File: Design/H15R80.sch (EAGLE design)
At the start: 24 parts, among them P1 HEXABIT_17.32_NO_P3_P6, U1 STM32F091CBU6, U2 DAC8760IRHAR, X1 XTALL_CSTCE8M00G52

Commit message: Finished schematics
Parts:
- added C12, C15: 10.0uF, rcl:CPOL-USCT7343
- added C13, C16, C18, C19, C20, C22, C25, C31, C33: 100nF, Hexabitz:C-0603
- added C14, C17, C21, C23, C24, C32, C34: 100pF, Hexabitz:C-0603
- added C26, C27, C28, C29: DNP, Hexabitz:C-0603
- added C30: 22nF, Hexabitz:C-0603
- added R5: 10.0K, Hexabitz:R-0603
- added R6: 15.0K, Hexabitz:R-0603
- added U3: OPA192, Hexabitz:OPA192IDBVR
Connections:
- removed net UART1_RX: U1.PA10
- removed net UART1_TX: U1.PA9
- removed net UART2_RX: U1.PA3
- removed net UART2_TX: U1.PA2
- new net +15V: C12.+, C13.1, C14.1, C20.1, C21.1, C26.2, C27.2, C31.1, C32.1, PWR-3.K, U2.AVDD, U3.V+
- new net -15V: C15.-, C16.1, C17.1, C22.1, C23.1, C24.1, C25.1, C33.1, C34.1, PWR-1.K, U2.AVSS, U2.AVSS_2, U2.PAD, U3.V-
- new net AGND: AO-2.K, C12.-, C13.2, C14.2, C15.+, C16.2, C17.2, C18.2, C19.2, C20.2, C21.2, C22.2, C23.2, C24.2, C25.2, C29.1, C30.2, C31.2, C32.2, C33.2, C34.2, PWR-2.K, R6.1, U2.-VSENSE, U2.CLR, U2.CLR-SEL, U2.DVDD-EN, U2.GND, U2.GND_2, U2.GND_3, U2.GND_4
- new net AO_ALARM: R5.1, U1.PA8, U2.ALARM_N
- new net N$1: AO-1.K, C28.2, C29.2, U2.IOUT, U2.VOUT, U3.IN+
- new net N$10: C27.1, U2.CAP1
- new net N$11: C28.1, U2.CMP
- new net N$12: R6.2, U2.ISET-R
- new net N$13: U2.+VSENSE, U3.IN-, U3.OUT
- new net N$14: C30.1, U2.HART-IN
- new net N$2: C19.1, U2.REFIN, U2.REFOUT
- new net N$8: C26.1, U2.CAP2
- new net SPI2_CS: U1.PB12, U2.LATCH
- new net SPI2_MISO: U1.PB14, U2.SDO
- new net SPI2_MOSI: U1.PB15, U2.DIN
- new net SPI2_SCK: U1.PB13, U2.SCLK
- new net UART1_RX*: P1.SD5, U1.PA10
- new net UART1_TX*: P1.SU5, U1.PA9
- new net UART2_RX*: P1.SD2, U1.PA3
- new net UART2_TX*: P1.SU2, U1.PA2
- net UART3_RX: now also P1.SD4
- net UART3_TX: now also P1.SU4
- net UART5_RX: now also P1.SD1
- net UART5_TX: now also P1.SU1
- net VDD: now also C18.1, R5.2, U2.DVDD
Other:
- note added: "Hi-precision Voltage & Current Analog Output"
- note removed: "Voltage & Current Analog Output"
- moved on the sheet: AO-1, AO-2, PWR-1, PWR-2, PWR-3

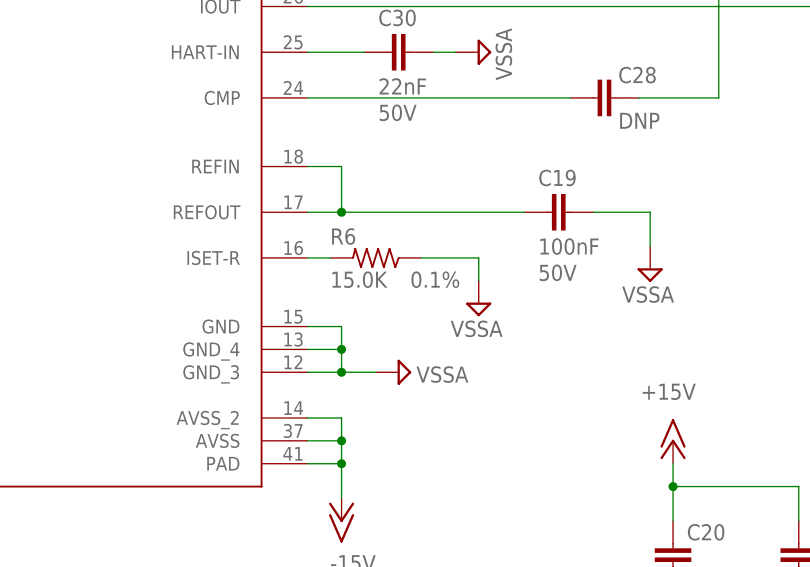
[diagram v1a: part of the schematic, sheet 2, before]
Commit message: Placed most components Routed analog routes
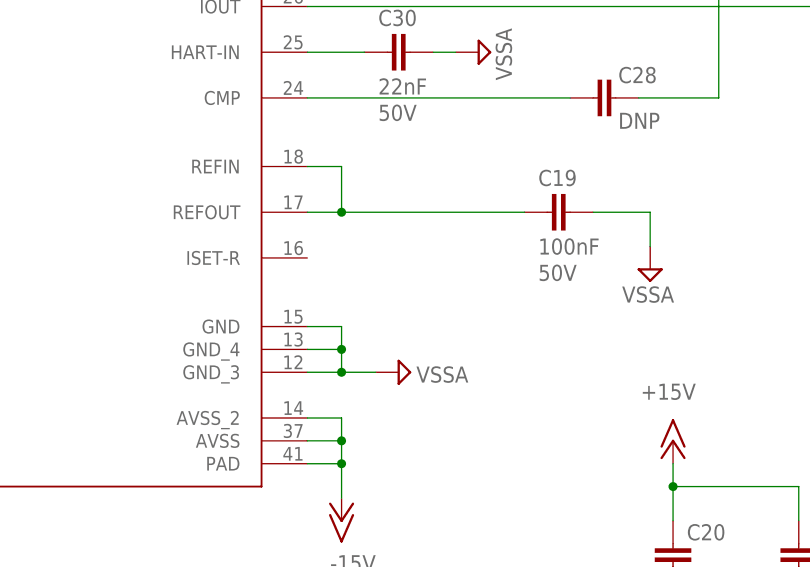
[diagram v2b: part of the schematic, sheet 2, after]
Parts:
- removed R6: 15.0K, Hexabitz:R-0603
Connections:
- removed net N$12: R6.2, U2.ISET-R
- net AGND: no longer R6.1
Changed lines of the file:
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@@
 <part name="SUPPLY28" library="supply2" deviceset="AGND" device="" value="VSSA"/>
 <part name="SUPPLY29" library="supply2" deviceset="AGND" device="" value="VSSA"/>
-<part name="R6" library="Hexabitz" deviceset="R-0603" device="" value="15.0K">
-<attribute name="MFN" value="Susumu"/>
-<attribute name="MPN" value="RG1608P-153-B-T5"/>
-<attribute name="OCTOPART_URL" value="https://octopart.com/rg1608p-153-b-t5-susumu-1191833?r=sp&amp;s=-o8BbZPwS5yNTzBtGupR8A"/>
-<attribute name="RESISTANCE" value="15.0 kOhm"/>
-<attribute name="TOLERANCE" value="0.1%"/>
-</part>
-<part name="SUPPLY30" library="supply2" deviceset="AGND" device="" value="VSSA"/>
 <part name="SUPPLY31" library="supply2" deviceset="AGND" device="" value="VSSA"/>
 <part name="C30" library="Hexabitz" deviceset="C-0603" device="" value="22nF">
@@
 <text x="116.84" y="95.25" size="1.778" layer="95">VDDA Coupling</text>
 <text x="153.67" y="95.25" size="1.778" layer="95">VDDIO2 Coupling</text>
-<text x="195.58" y="95.25" size="1.778" layer="95">VDD Coupling</text>
+<text x="193.04" y="95.25" size="1.778" layer="95">VDD Coupling</text>
 <text x="229.87" y="95.25" size="1.778" layer="95">VBAT</text>
 <text x="0" y="-0.127" size="0.0508" layer="205" font="vector">C:/Users/Admin/Desktop/logodraft.bmp</text>
@@
 </instance>
 <instance part="SUPPLY8" gate="G$1" x="156.21" y="87.63" smashed="yes">
-<attribute name="VALUE" x="159.385" y="92.075" size="1.778" layer="96" rot="R180"/>
+<attribute name="VALUE" x="154.305" y="90.805" size="1.778" layer="96"/>
 </instance>
 <instance part="GND2" gate="1" x="156.21" y="69.85" smashed="yes">
@@
 </instance>
 <instance part="SUPPLY10" gate="G$1" x="190.5" y="87.63" smashed="yes">
-<attribute name="VALUE" x="193.675" y="92.075" size="1.778" layer="96" rot="R180"/>
+<attribute name="VALUE" x="188.595" y="90.805" size="1.778" layer="96"/>
 </instance>
 <instance part="SUPPLY13" gate="G$1" x="232.41" y="87.63" smashed="yes">
-<attribute name="VALUE" x="235.585" y="92.075" size="1.778" layer="96" rot="R180"/>
+<attribute name="VALUE" x="230.505" y="90.805" size="1.778" layer="96"/>
 </instance>
 <instance part="SUPPLY12" gate="G$1" x="203.2" y="109.22" smashed="yes" rot="R90">
@@
 <attribute name="VALUE" x="93.345" y="142.113" size="1.778" layer="96" rot="R90"/>
 </instance>
-<instance part="R6" gate="G$1" x="156.21" y="81.28" smashed="yes" rot="R180">
-<attribute name="NAME" x="151.13" y="82.7786" size="1.778" layer="95"/>
-<attribute name="VALUE" x="151.13" y="77.978" size="1.778" layer="96"/>
-<attribute name="TOLERANCE" x="160.02" y="77.978" size="1.778" layer="96"/>
-</instance>
-<instance part="SUPPLY30" gate="G$1" x="167.64" y="76.2" smashed="yes">
-<attribute name="VALUE" x="170.307" y="74.295" size="1.778" layer="96" rot="R180"/>
-</instance>
 <instance part="SUPPLY31" gate="G$1" x="158.75" y="144.78" smashed="yes" rot="R90">
 <attribute name="VALUE" x="160.655" y="147.447" size="1.778" layer="96" rot="R270"/>
@@
 </segment>
 <segment>
-<pinref part="R6" gate="G$1" pin="1"/>
-<pinref part="SUPPLY30" gate="G$1" pin="AGND"/>
-<wire x1="167.64" y1="78.74" x2="167.64" y2="81.28" width="0.1524" layer="91"/>
-<wire x1="167.64" y1="81.28" x2="161.29" y2="81.28" width="0.1524" layer="91"/>
-</segment>
-<segment>
 <pinref part="U2" gate="A" pin="-VSENSE"/>
 <pinref part="SUPPLY31" gate="G$1" pin="AGND"/>
@@
 </segment>
 </net>
-<net name="N$12" class="0">
-<segment>
-<pinref part="U2" gate="A" pin="ISET-R"/>
-<pinref part="R6" gate="G$1" pin="2"/>
-<wire x1="151.13" y1="81.28" x2="148.59" y2="81.28" width="0.1524" layer="91"/>
-</segment>
-</net>
 <net name="N$13" class="0">
 <segment>
@@
 </sheet>
 </sheets>
+<errors>
+</errors>
 </schematic>
 </drawing>

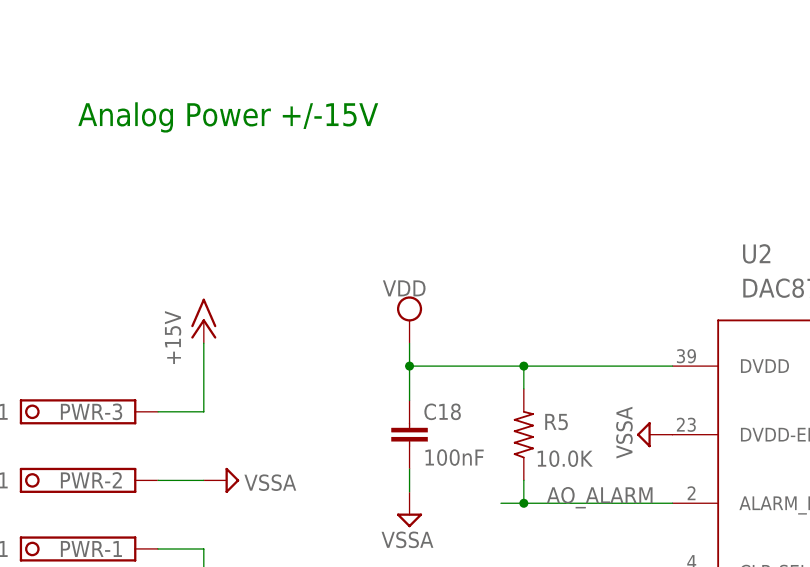
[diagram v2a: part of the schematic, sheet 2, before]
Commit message: Routing digital section
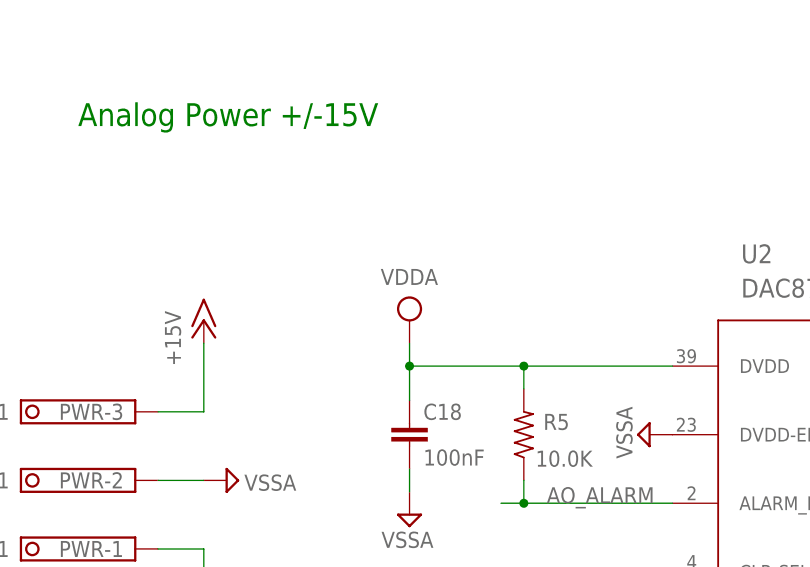
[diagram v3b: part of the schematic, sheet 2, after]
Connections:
- removed net AGND: AO-2.K, C12.-, C13.2, C14.2, C15.+, C16.2, C17.2, C18.2, C19.2, C20.2, C21.2, C22.2, C23.2, C24.2, C25.2, C29.1, C30.2, C31.2, C32.2, C33.2, C34.2, PWR-2.K, U2.-VSENSE, U2.CLR, U2.CLR-SEL, U2.DVDD-EN, U2.GND, U2.GND_2, U2.GND_3, U2.GND_4
- net VDD: no longer C18.1, R5.2, U2.DVDD
- net VDDA: now also C18.1, R5.2, U2.DVDD
- net VSSA: now also AO-2.K, C12.-, C13.2, C14.2, C15.+, C16.2, C17.2, C18.2, C19.2, C20.2, C21.2, C22.2, C23.2, C24.2, C25.2, C29.1, C30.2, C31.2, C32.2, C33.2, C34.2, PWR-2.K, U2.-VSENSE, U2.CLR, U2.CLR-SEL, U2.DVDD-EN, U2.GND, U2.GND_2, U2.GND_3, U2.GND_4
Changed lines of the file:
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@@
 <attribute name="VOLTAGE_RATING" value="10V"/>
 </part>
-<part name="SUPPLY20" library="supply2" deviceset="VDD" device=""/>
 <part name="R5" library="Hexabitz" deviceset="R-0603" device="" value="10.0K">
 <attribute name="MFN" value="Yageo"/>
@@
 <part name="SUPPLY34" library="supply2" deviceset="AGND" device="" value="VSSA"/>
 <part name="P-6" library="supply1" library_urn="urn:adsk.eagle:library:371" deviceset="-15V" device=""/>
+<part name="SUPPLY14" library="supply2" deviceset="VCC" device="" value="VDDA"/>
 </parts>
 <sheets>
@@
 <attribute name="VALUE" x="70.104" y="141.351" size="1.778" layer="96"/>
 </instance>
-<instance part="SUPPLY20" gate="G$1" x="68.58" y="157.48" smashed="yes">
-<attribute name="VALUE" x="70.485" y="161.925" size="1.778" layer="96" rot="R180"/>
-</instance>
 <instance part="R5" gate="G$1" x="81.28" y="144.78" smashed="yes" rot="R90">
 <attribute name="NAME" x="86.36" y="147.0914" size="1.778" layer="95" rot="R180"/>
@@
 <attribute name="VALUE" x="246.38" y="176.53" size="1.778" layer="96"/>
 </instance>
+<instance part="SUPPLY14" gate="G$1" x="68.58" y="157.48" smashed="yes">
+<attribute name="VALUE" x="71.755" y="163.195" size="1.778" layer="96" rot="R180"/>
+</instance>
 </instances>
 <busses>
@@
 </segment>
 </net>
-<net name="AGND" class="0">
+<net name="VSSA" class="0">
 <segment>
 <pinref part="PWR" gate="-2" pin="K"/>
@@
 </segment>
 </net>
-<net name="VDD" class="0">
-<segment>
-<pinref part="SUPPLY20" gate="G$1" pin="VDD"/>
-<pinref part="C18" gate="G$1" pin="1"/>
-<wire x1="68.58" y1="154.94" x2="68.58" y2="152.4" width="0.1524" layer="91"/>
-<pinref part="U2" gate="A" pin="DVDD"/>
-<wire x1="68.58" y1="152.4" x2="68.58" y2="148.59" width="0.1524" layer="91"/>
-<wire x1="97.79" y1="152.4" x2="81.28" y2="152.4" width="0.1524" layer="91"/>
-<junction x="68.58" y="152.4"/>
-<pinref part="R5" gate="G$1" pin="2"/>
-<wire x1="81.28" y1="152.4" x2="68.58" y2="152.4" width="0.1524" layer="91"/>
-<wire x1="81.28" y1="149.86" x2="81.28" y2="152.4" width="0.1524" layer="91"/>
-<junction x="81.28" y="152.4"/>
-</segment>
-</net>
 <net name="AO_ALARM" class="0">
 <segment>
@@
 </segment>
 </net>
+<net name="VDDA" class="0">
+<segment>
+<pinref part="C18" gate="G$1" pin="1"/>
+<wire x1="68.58" y1="154.94" x2="68.58" y2="152.4" width="0.1524" layer="91"/>
+<pinref part="U2" gate="A" pin="DVDD"/>
+<wire x1="68.58" y1="152.4" x2="68.58" y2="148.59" width="0.1524" layer="91"/>
+<wire x1="97.79" y1="152.4" x2="81.28" y2="152.4" width="0.1524" layer="91"/>
+<junction x="68.58" y="152.4"/>
+<pinref part="R5" gate="G$1" pin="2"/>
+<wire x1="81.28" y1="152.4" x2="68.58" y2="152.4" width="0.1524" layer="91"/>
+<wire x1="81.28" y1="149.86" x2="81.28" y2="152.4" width="0.1524" layer="91"/>
+<junction x="81.28" y="152.4"/>
+<pinref part="SUPPLY14" gate="G$1" pin="VCC"/>
+</segment>
+</net>

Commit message: Finished routing and silkscreen placement
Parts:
- U2: value DAC8760IRHAR -> DAC8760RHA
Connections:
- net GND: now also U1.PA15, U1.PA6, U1.PA7, U1.PB0, U1.PB1, U1.PB2, U1.PB5, U1.PB6, U1.PB7, U1.PC13, U1.PC14-OSC32_IN, U1.PC15-OSC32_OUT
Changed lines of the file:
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@@
 <attribute name="OCTOPART_URL" value="https://octopart.com/1751251-phoenix+contact-36473?r=sp&amp;s=9M0VWNoHTyq04j3qI6lQOQ "/>
 </part>
-<part name="U2" library="Hexabitz" deviceset="DAC7760IRHAR" device="" value="DAC8760IRHAR"/>
+<part name="U2" library="Hexabitz" deviceset="DAC7760IRHAR" device="" value="DAC8760RHA"/>
 <part name="SUPPLY15" library="supply2" deviceset="AGND" device="" value="VSSA"/>
 <part name="P+1" library="supply1" library_urn="urn:adsk.eagle:library:371" deviceset="+15V" device=""/>
@@
 <part name="P-6" library="supply1" library_urn="urn:adsk.eagle:library:371" deviceset="-15V" device=""/>
 <part name="SUPPLY14" library="supply2" deviceset="VCC" device="" value="VDDA"/>
+<part name="GND9" library="supply1" deviceset="GND" device=""/>
+<part name="GND10" library="supply1" deviceset="GND" device=""/>
+<part name="GND11" library="supply1" deviceset="GND" device=""/>
+<part name="GND12" library="supply1" deviceset="GND" device=""/>
 </parts>
 <sheets>
@@
 <attribute name="VALUE" x="43.815" y="98.425" size="1.778" layer="96"/>
 </instance>
+<instance part="GND9" gate="1" x="120.65" y="162.56" smashed="yes" rot="R270">
+<attribute name="VALUE" x="118.11" y="165.1" size="1.778" layer="96" rot="R270"/>
+</instance>
+<instance part="GND10" gate="1" x="198.12" y="177.8" smashed="yes" rot="R90">
+<attribute name="VALUE" x="200.66" y="175.26" size="1.778" layer="96" rot="R90"/>
+</instance>
+<instance part="GND11" gate="1" x="129.54" y="132.08" smashed="yes" rot="R270">
+<attribute name="VALUE" x="127" y="134.62" size="1.778" layer="96" rot="R270"/>
+</instance>
+<instance part="GND12" gate="1" x="198.12" y="162.56" smashed="yes" rot="R90">
+<attribute name="VALUE" x="200.66" y="160.02" size="1.778" layer="96" rot="R90"/>
+</instance>
 </instances>
 <busses>
@@
 <junction x="45.72" y="111.76"/>
 </segment>
+<segment>
+<pinref part="GND9" gate="1" pin="GND"/>
+<pinref part="U1" gate="G$1" pin="PA6"/>
+<wire x1="123.19" y1="162.56" x2="134.62" y2="162.56" width="0.1524" layer="91"/>
+<pinref part="U1" gate="G$1" pin="PA7"/>
+<wire x1="134.62" y1="162.56" x2="135.89" y2="162.56" width="0.1524" layer="91"/>
+<wire x1="135.89" y1="160.02" x2="134.62" y2="160.02" width="0.1524" layer="91"/>
+<wire x1="134.62" y1="160.02" x2="134.62" y2="162.56" width="0.1524" layer="91"/>
+<junction x="134.62" y="162.56"/>
+</segment>
+<segment>
+<pinref part="GND10" gate="1" pin="GND"/>
+<pinref part="U1" gate="G$1" pin="PB0"/>
+<wire x1="195.58" y1="177.8" x2="193.04" y2="177.8" width="0.1524" layer="91"/>
+<pinref part="U1" gate="G$1" pin="PB2"/>
+<wire x1="193.04" y1="177.8" x2="191.77" y2="177.8" width="0.1524" layer="91"/>
+<wire x1="191.77" y1="172.72" x2="193.04" y2="172.72" width="0.1524" layer="91"/>
+<wire x1="193.04" y1="172.72" x2="193.04" y2="175.26" width="0.1524" layer="91"/>
+<junction x="193.04" y="177.8"/>
+<pinref part="U1" gate="G$1" pin="PB1"/>
+<wire x1="193.04" y1="175.26" x2="193.04" y2="177.8" width="0.1524" layer="91"/>
+<wire x1="191.77" y1="175.26" x2="193.04" y2="175.26" width="0.1524" layer="91"/>
+<junction x="193.04" y="175.26"/>
+</segment>
+<segment>
+<pinref part="GND11" gate="1" pin="GND"/>
+<pinref part="U1" gate="G$1" pin="PC15-OSC32_OUT"/>
+<wire x1="132.08" y1="132.08" x2="134.62" y2="132.08" width="0.1524" layer="91"/>
+<pinref part="U1" gate="G$1" pin="PC13"/>
+<wire x1="134.62" y1="132.08" x2="135.89" y2="132.08" width="0.1524" layer="91"/>
+<wire x1="135.89" y1="134.62" x2="134.62" y2="134.62" width="0.1524" layer="91"/>
+<wire x1="134.62" y1="134.62" x2="134.62" y2="132.08" width="0.1524" layer="91"/>
+<junction x="134.62" y="132.08"/>
+<pinref part="U1" gate="G$1" pin="PC14-OSC32_IN"/>
+<wire x1="135.89" y1="129.54" x2="134.62" y2="129.54" width="0.1524" layer="91"/>
+<wire x1="134.62" y1="129.54" x2="134.62" y2="132.08" width="0.1524" layer="91"/>
+<pinref part="U1" gate="G$1" pin="PA15"/>
+<wire x1="135.89" y1="139.7" x2="134.62" y2="139.7" width="0.1524" layer="91"/>
+<wire x1="134.62" y1="139.7" x2="134.62" y2="134.62" width="0.1524" layer="91"/>
+<junction x="134.62" y="134.62"/>
+</segment>
+<segment>
+<pinref part="U1" gate="G$1" pin="PB7"/>
+<wire x1="191.77" y1="160.02" x2="193.04" y2="160.02" width="0.1524" layer="91"/>
+<wire x1="193.04" y1="160.02" x2="193.04" y2="162.56" width="0.1524" layer="91"/>
+<pinref part="U1" gate="G$1" pin="PB5"/>
+<wire x1="193.04" y1="162.56" x2="193.04" y2="165.1" width="0.1524" layer="91"/>
+<wire x1="193.04" y1="165.1" x2="191.77" y2="165.1" width="0.1524" layer="91"/>
+<pinref part="U1" gate="G$1" pin="PB6"/>
+<wire x1="191.77" y1="162.56" x2="193.04" y2="162.56" width="0.1524" layer="91"/>
+<junction x="193.04" y="162.56"/>
+<pinref part="GND12" gate="1" pin="GND"/>
+<wire x1="195.58" y1="162.56" x2="193.04" y2="162.56" width="0.1524" layer="91"/>
+</segment>
 </net>

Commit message: Added BOM. Release V0
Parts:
- U3: MFN (none) -> Texas Instruments; MPN (none) -> OPA192IDBVR; OCTOPART_URL (none) -> https://octopart.com/opa192idbvr-texas+instruments-33513820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
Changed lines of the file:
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@@
 </part>
 <part name="SUPPLY32" library="supply2" deviceset="AGND" device="" value="VSSA"/>
-<part name="U3" library="Hexabitz" deviceset="OPA192IDBVR" device="" value="OPA192"/>
+<part name="U3" library="Hexabitz" deviceset="OPA192IDBVR" device="" value="OPA192">
+<attribute name="MFN" value="Texas Instruments"/>
+<attribute name="MPN" value="OPA192IDBVR"/>
+<attribute name="OCTOPART_URL" value="https://octopart.com/opa192idbvr-texas+instruments-33513820?r=sp&amp;s=D6KF1OAATrGkqNyouFfzCw"/>
+</part>
 <part name="P+6" library="supply1" library_urn="urn:adsk.eagle:library:371" deviceset="+15V" device=""/>
 <part name="P-5" library="supply1" library_urn="urn:adsk.eagle:library:371" deviceset="-15V" device=""/>
@@
 <attribute name="NAME" x="191.77" y="166.37" size="2.0828" layer="95" rot="SMR180"/>
 <attribute name="VALUE" x="191.77" y="163.83" size="2.0828" layer="96" rot="SMR180"/>
+<attribute name="MFN" x="194.31" y="160.02" size="1.778" layer="96" rot="MR0" display="off"/>
+<attribute name="MPN" x="194.31" y="160.02" size="1.778" layer="96" rot="MR0" display="off"/>
+<attribute name="OCTOPART_URL" x="194.31" y="160.02" size="1.778" layer="96" rot="MR0" display="off"/>
 </instance>
 <instance part="P+6" gate="1" x="189.23" y="167.64" smashed="yes">
